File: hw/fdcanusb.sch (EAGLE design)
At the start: 37 parts, among them J3 JST-ZH6SMT_VERT, M1 MOUNT, M2 MOUNT, M3 MOUNT, M4 MOUNT, U1 MF-REG-SOT235-3.3V-300mA, U2 USBLC6-2SC6, U3 TCAN334GSOT23, U4 TLP3317, U5 STM32G474CEU6

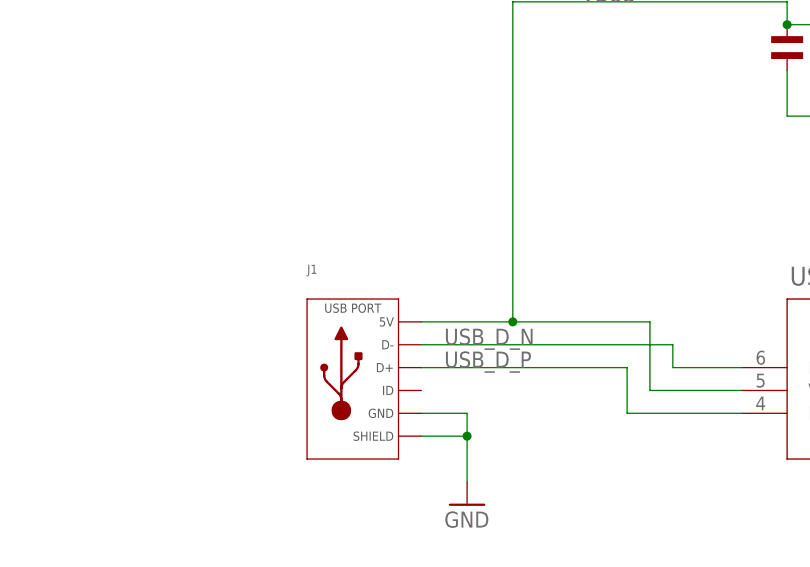
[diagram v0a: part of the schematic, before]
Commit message: Switch to actually using a micro USB connector
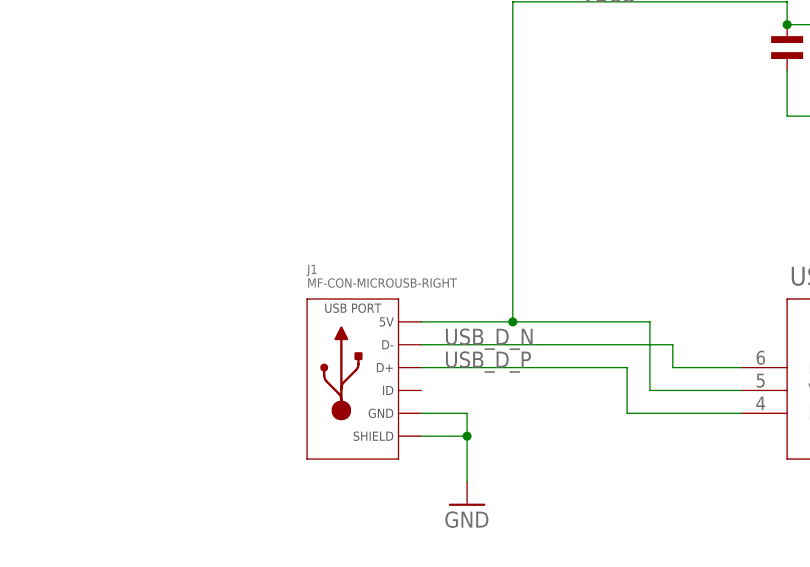
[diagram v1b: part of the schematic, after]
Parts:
- J1: value (none) -> MF-CON-MICROUSB-RIGHT; device mfconnectors:USB_MINI_RIGHT -> mfconnectors:USB_MICRO_RIGHT; HUOSEPART YES -> (none); MPN MF-CON-MICROUSB-RIGHT -> (none)
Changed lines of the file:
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@@
 <attribute name="POPULATE" value="0"/>
 </part>
-<part name="J1" library="mfconnectors" deviceset="USB" device="_MINI_RIGHT">
-<attribute name="HUOSEPART" value="YES"/>
-<attribute name="MPN" value="MF-CON-MICROUSB-RIGHT"/>
-</part>
+<part name="J1" library="mfconnectors" deviceset="USB" device="_MICRO_RIGHT" value="MF-CON-MICROUSB-RIGHT"/>
 <part name="U1" library="mficpower" deviceset="TLV702" device="33PDBVR" value="MF-REG-SOT235-3.3V-300mA"/>
 <part name="C1" library="mfpassives" deviceset="CAPACITOR_NP" device="_0603" value="1uF">

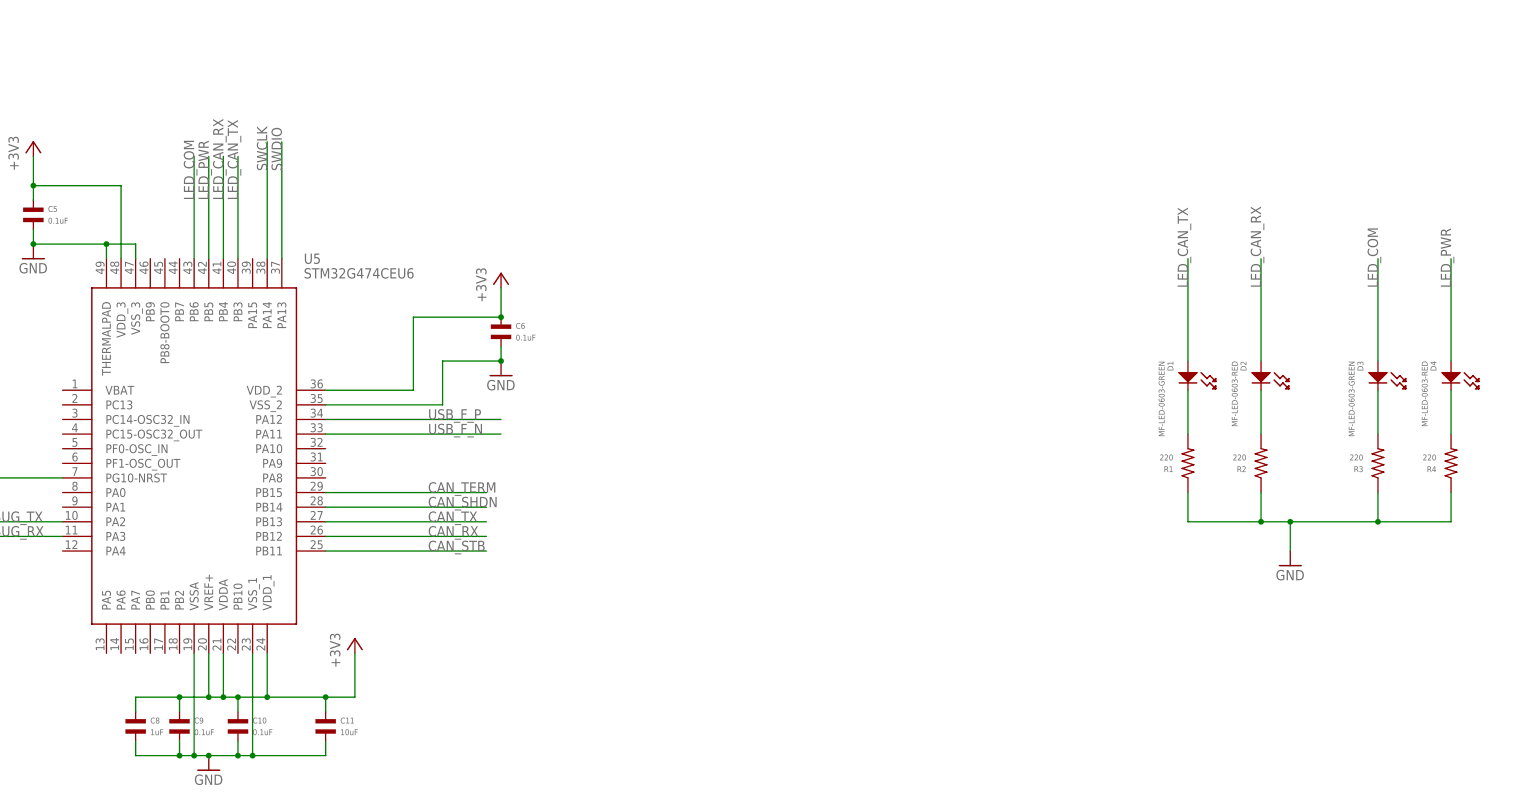
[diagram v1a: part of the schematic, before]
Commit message: Update to use correct STM32 pinout
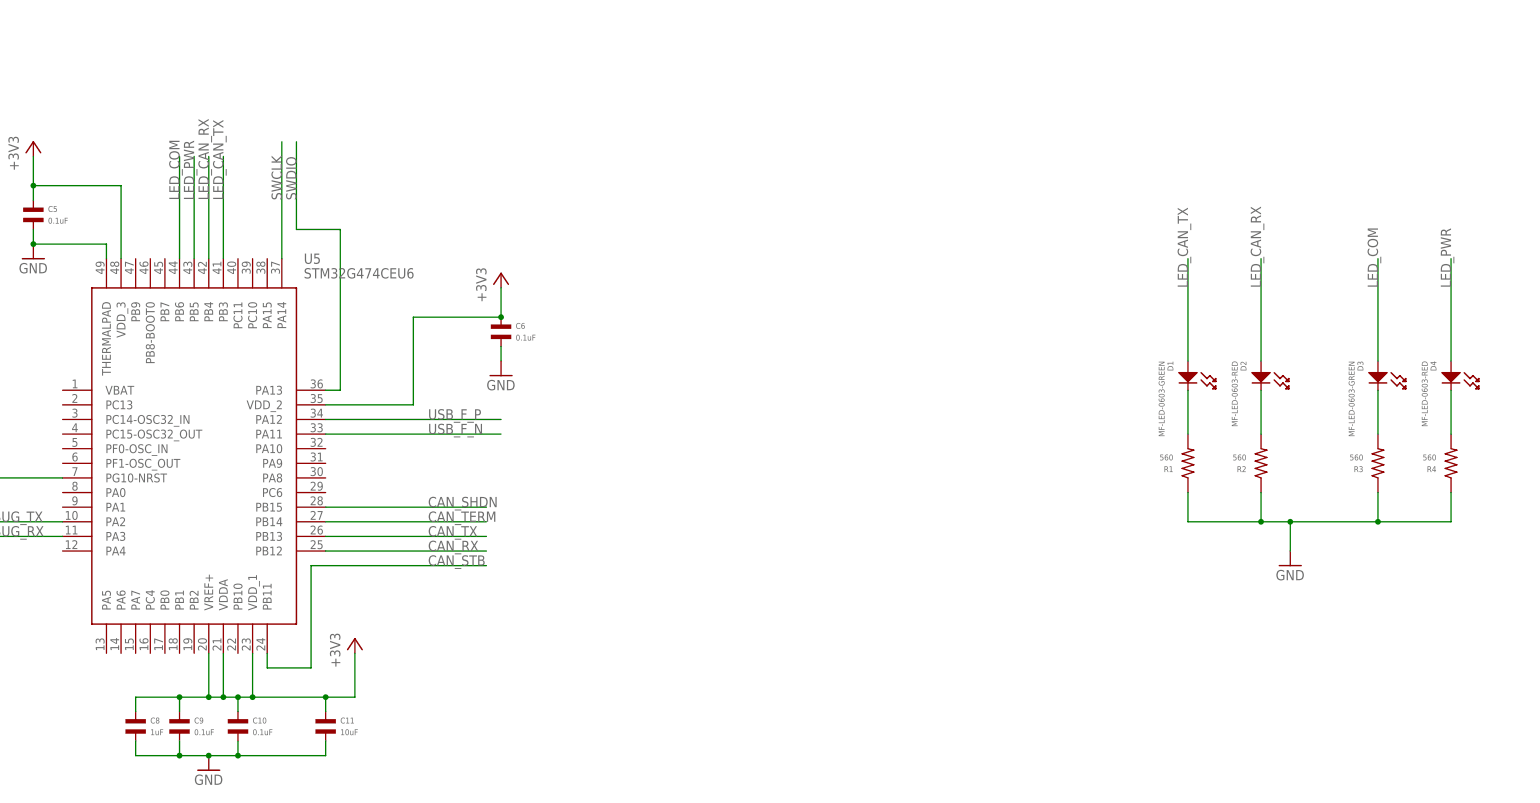
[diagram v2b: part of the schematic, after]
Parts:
- J2: MF (none) -> Assmann WSW Components; MPN (none) -> A-DS 09 A/KG-T2S; POPULATE 0 -> 1
- R1, R2, R3, R4: value 220 -> 560; MPN MF-RES-0402-220 -> MF-RES-0402-560
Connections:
- net CAN_SHDN: now also U5.PB15; no longer U5.PB14
- net CAN_TERM: now also U5.PB14; no longer U5.PB15
- net GND: no longer U5.VSSA, U5.VSS_1, U5.VSS_2, U5.VSS_3
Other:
- note added: "fdcanusb r2 (c) 2019 Josh Pieper, jjp@pobox.com Licensed under the Apache 2.0 License https://www.apache.org/licenses/LICENSE-2.0"
- note removed: "fdcanusb (c) 2019 Josh Pieper, jjp@pobox.com Licensed under the Apache 2.0 License https://www.apache.org/licenses/LICENSE-2.0"

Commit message: Use the digikey number for DB9, since MF can find it
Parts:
- J2: MPN A-DS 09 A/KG-T2S -> AE10968-ND
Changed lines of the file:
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@@
 <part name="J2" library="fdcanusb" deviceset="F09" device="H">
 <attribute name="MF" value="Assmann WSW Components"/>
-<attribute name="MPN" value="A-DS 09 A/KG-T2S"/>
+<attribute name="MPN" value="AE10968-ND"/>
 <attribute name="POPULATE" value="1"/>
 </part>

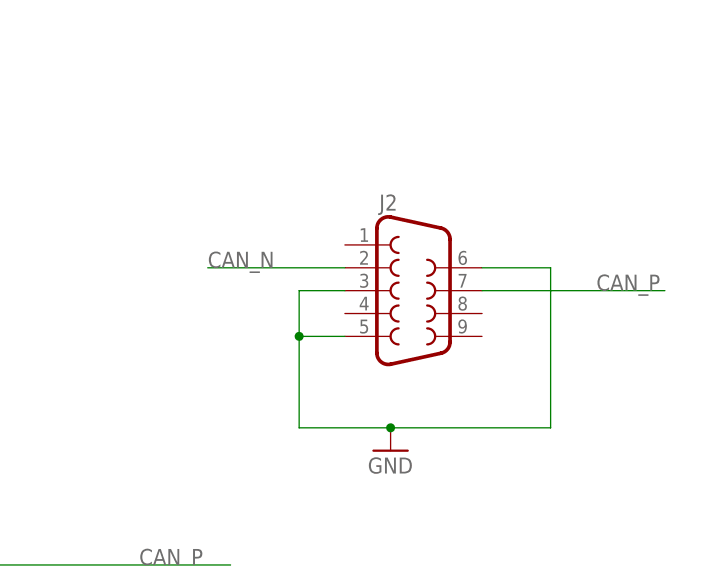
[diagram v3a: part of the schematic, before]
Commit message: Fix DB9 pinout
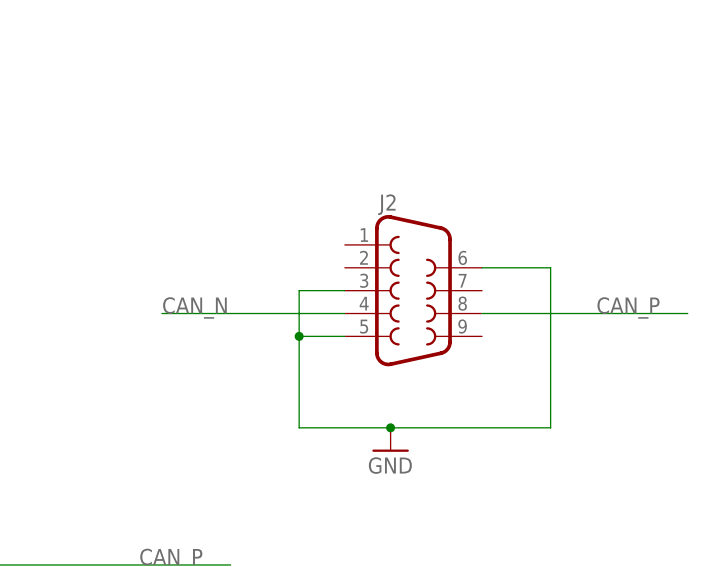
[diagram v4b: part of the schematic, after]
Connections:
- net CAN_N: now also J2.4; no longer J2.2
- net CAN_P: now also J2.8; no longer J2.7
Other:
- note added: "fdcanusb r2.1 (c) 2019 Josh Pieper, jjp@pobox.com Licensed under the Apache 2.0 License https://www.apache.org/licenses/LICENSE-2.0"
- note removed: "fdcanusb r2 (c) 2019 Josh Pieper, jjp@pobox.com Licensed under the Apache 2.0 License https://www.apache.org/licenses/LICENSE-2.0"
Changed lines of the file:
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@@
 <wire x1="-5.08" y1="-63.5" x2="-5.08" y2="88.9" width="0.1524" layer="90"/>
 <text x="0" y="73.66" size="7.62" layer="90">MOUNTS / POWER</text>
-<text x="-5.08" y="93.98" size="3.81" layer="90">fdcanusb r2
+<text x="-5.08" y="93.98" size="3.81" layer="90">fdcanusb r2.1
 (c) 2019 Josh Pieper, jjp@pobox.com
 Licensed under the Apache 2.0 License
@@
 <net name="CAN_N" class="2">
 <segment>
-<pinref part="J2" gate="G$1" pin="2"/>
-<wire x1="449.58" y1="17.78" x2="434.34" y2="17.78" width="0.1524" layer="91"/>
-<label x="434.34" y="17.78" size="1.778" layer="95"/>
-</segment>
-<segment>
 <pinref part="U3" gate="G$1" pin="CANL"/>
 <wire x1="370.84" y1="43.18" x2="401.32" y2="43.18" width="0.1524" layer="91"/>
@@
 <wire x1="398.78" y1="-45.72" x2="406.4" y2="-45.72" width="0.1524" layer="91"/>
 </segment>
+<segment>
+<pinref part="J2" gate="G$1" pin="4"/>
+<wire x1="449.58" y1="12.7" x2="429.26" y2="12.7" width="0.1524" layer="91"/>
+<label x="429.26" y="12.7" size="1.778" layer="95"/>
+</segment>
 </net>
 <net name="CAN_P" class="2">
-<segment>
-<pinref part="J2" gate="G$1" pin="7"/>
-<wire x1="464.82" y1="15.24" x2="485.14" y2="15.24" width="0.1524" layer="91"/>
-<label x="477.52" y="15.24" size="1.778" layer="95"/>
-</segment>
 <segment>
 <pinref part="U3" gate="G$1" pin="CANH"/>
@@
 <label x="426.72" y="-15.24" size="1.778" layer="95"/>
 </segment>
-</net>
+<segment>
+<pinref part="J2" gate="G$1" pin="8"/>
+<wire x1="464.82" y1="12.7" x2="487.68" y2="12.7" width="0.1524" layer="91"/>
+<label x="477.52" y="12.7" size="1.778" layer="95"/>
+</segment>
+</net>

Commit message: Update to r2.2
This just reduces the size of the PCB so it doesn't hang out so far
under the DB-9 connector.
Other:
- note added: "mjbots fdcanusb r2.2 (c) 2020 Josh Pieper, jpieper@mjbots.com Licensed under the Apache 2.0 License https://www.apache.org/licenses/LICENSE-2.0"
- note removed: "fdcanusb r2.1 (c) 2019 Josh Pieper, jjp@pobox.com Licensed under the Apache 2.0 License https://www.apache.org/licenses/LICENSE-2.0"
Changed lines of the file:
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@@
 <wire x1="-5.08" y1="-63.5" x2="-5.08" y2="88.9" width="0.1524" layer="90"/>
 <text x="0" y="73.66" size="7.62" layer="90">MOUNTS / POWER</text>
-<text x="-5.08" y="93.98" size="3.81" layer="90">fdcanusb r2.1
-(c) 2019 Josh Pieper, jjp@pobox.com
+<text x="-5.08" y="93.98" size="3.81" layer="90">mjbots fdcanusb r2.2
+(c) 2020 Josh Pieper, jpieper@mjbots.com
 Licensed under the Apache 2.0 License
 https://www.apache.org/licenses/LICENSE-2.0</text>

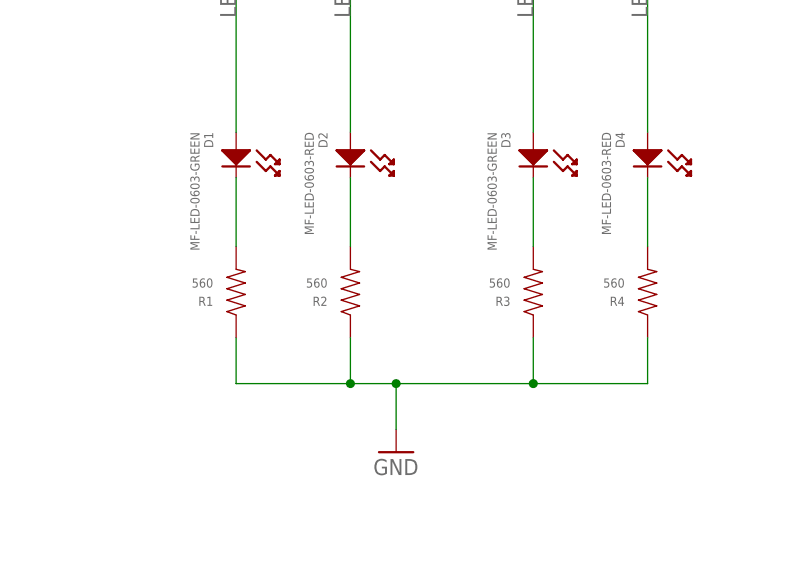
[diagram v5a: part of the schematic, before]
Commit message: Switch LED resistors back to 220s
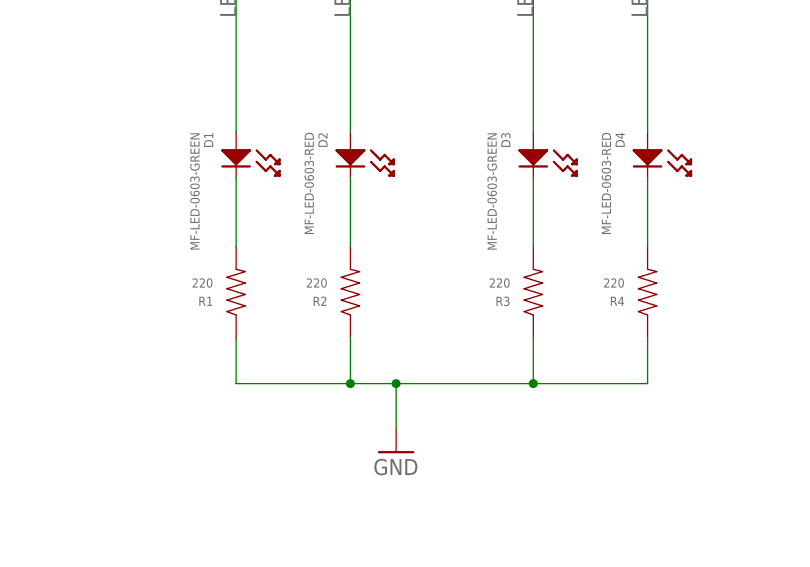
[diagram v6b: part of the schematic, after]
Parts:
- R1, R2, R3, R4: value 560 -> 220; MPN MF-RES-0402-560 -> MF-RES-0402-220
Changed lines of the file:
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@@
 <part name="D2" library="mfleds" deviceset="LED_SINGLE" device="-0603-RED" value="MF-LED-0603-RED"/>
 <part name="D4" library="mfleds" deviceset="LED_SINGLE" device="-0603-RED" value="MF-LED-0603-RED"/>
-<part name="R1" library="mfpassives" deviceset="RESISTOR" device="_0402" value="560">
-<attribute name="MPN" value="MF-RES-0402-560"/>
+<part name="R1" library="mfpassives" deviceset="RESISTOR" device="_0402" value="220">
+<attribute name="MPN" value="MF-RES-0402-220"/>
 </part>
-<part name="R2" library="mfpassives" deviceset="RESISTOR" device="_0402" value="560">
-<attribute name="MPN" value="MF-RES-0402-560"/>
+<part name="R2" library="mfpassives" deviceset="RESISTOR" device="_0402" value="220">
+<attribute name="MPN" value="MF-RES-0402-220"/>
 </part>
-<part name="R3" library="mfpassives" deviceset="RESISTOR" device="_0402" value="560">
-<attribute name="MPN" value="MF-RES-0402-560"/>
+<part name="R3" library="mfpassives" deviceset="RESISTOR" device="_0402" value="220">
+<attribute name="MPN" value="MF-RES-0402-220"/>
 </part>
-<part name="R4" library="mfpassives" deviceset="RESISTOR" device="_0402" value="560">
-<attribute name="MPN" value="MF-RES-0402-560"/>
+<part name="R4" library="mfpassives" deviceset="RESISTOR" device="_0402" value="220">
+<attribute name="MPN" value="MF-RES-0402-220"/>
 </part>
 <part name="GND11" library="supply1" deviceset="GND" device=""/>

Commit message: Make DB9 have plated holes for retaining clips
This should improve the mechanical strength of the DB9 connector when
installed
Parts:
- J2: device fdcanusb:F09H -> fdcanusb:F09; MF Assmann WSW Components -> (none); MPN AE10968-ND -> (none)
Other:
- note added: "mjbots fdcanusb r2.3 (c) 2021 Josh Pieper, jpieper@mjbots.com Licensed under the Apache 2.0 License https://www.apache.org/licenses/LICENSE-2.0"
- note removed: "mjbots fdcanusb r2.2 (c) 2020 Josh Pieper, jpieper@mjbots.com Licensed under the Apache 2.0 License https://www.apache.org/licenses/LICENSE-2.0"
